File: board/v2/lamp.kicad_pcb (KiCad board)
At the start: 4 copper layers, 28 x 28 mm, 42 parts, among them J1 Conn_01x01_Female, J2 Conn_01x01_Female, J3 Conn_01x01_Female, J4 Conn_01x01_Female, J5 Conn_01x01_Female, J6 Conn_01x01_Female, J7 Conn_01x01_Female, J8 Conn_ARM_JTAG_SWD_10, Q1 SIA483DJ-T1-GE3‎, U1 STM32G071GxU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

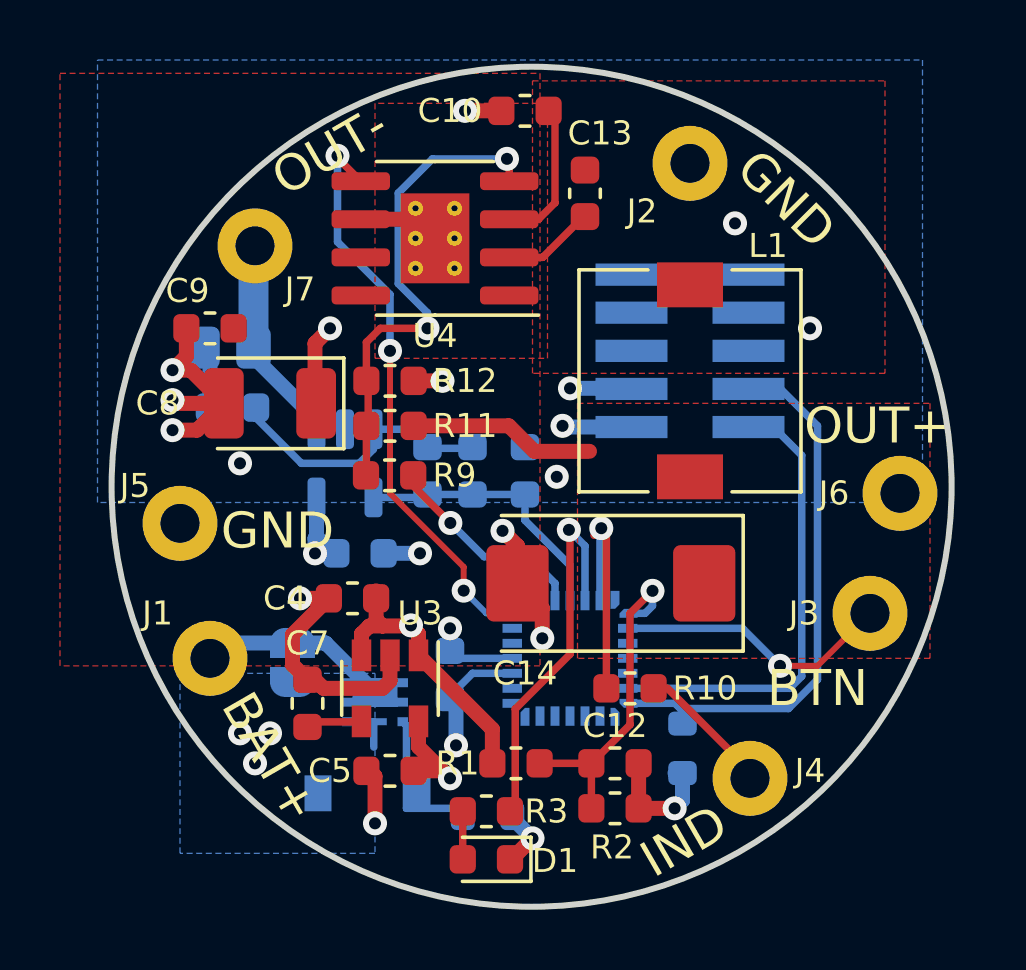
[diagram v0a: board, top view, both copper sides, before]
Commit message: hw: Fix RESET line on JTAG connector
Previously this was disconnected due to a net name mismatch.
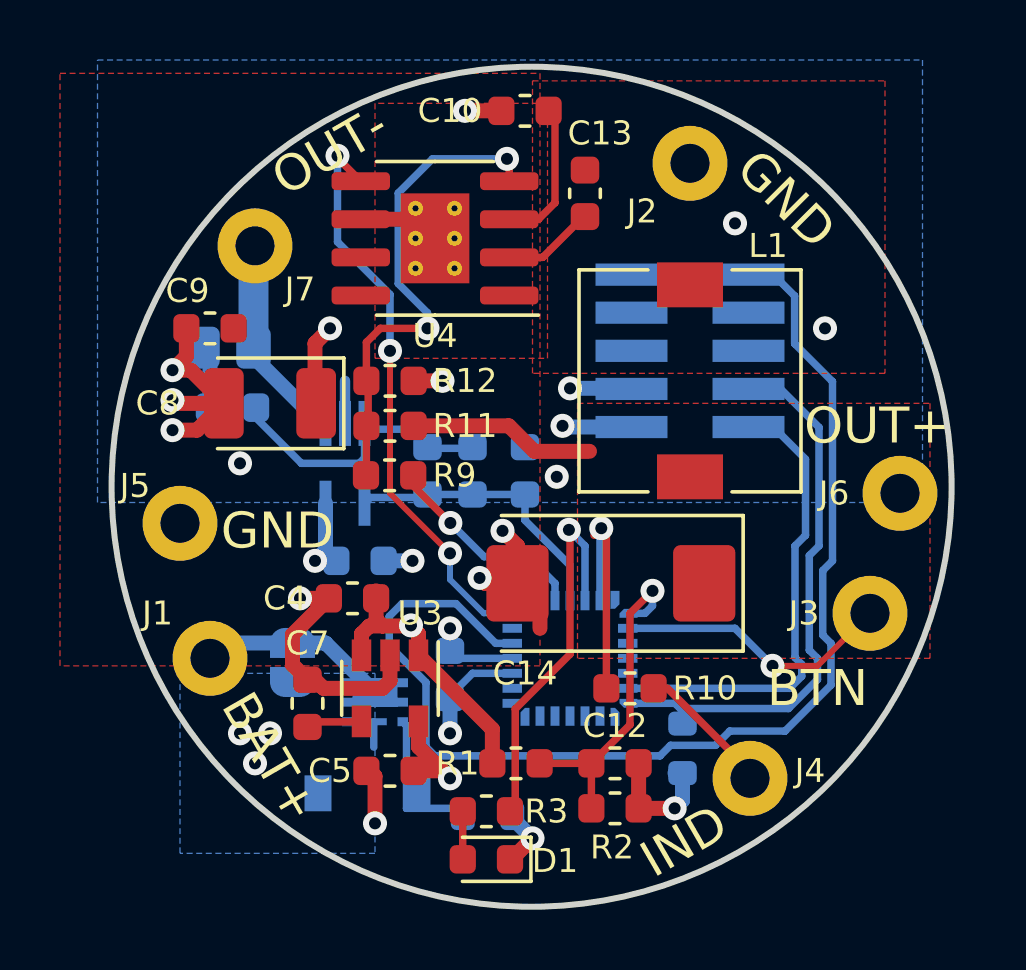
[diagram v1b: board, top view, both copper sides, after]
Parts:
- U2: footprint Package_TO_SOT_SMD:SOT-23-5 -> Package_TO_SOT_SMD:SOT-353_SC-70-5_Handsoldering
- moved C11 0.25 mm to (130.0, 86.2)
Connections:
- U1 pad 5: /RESET -> /~{RESET}
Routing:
- net /~{RESET}: track 0.00 -> 39.9 mm
- net GND: track 40.0 -> 42.2 mm
- net +3V3: track 13.9 -> 13.2 mm

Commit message: hw: Larger package for LDO input cap
0603 was too small for a realistic capacitance.
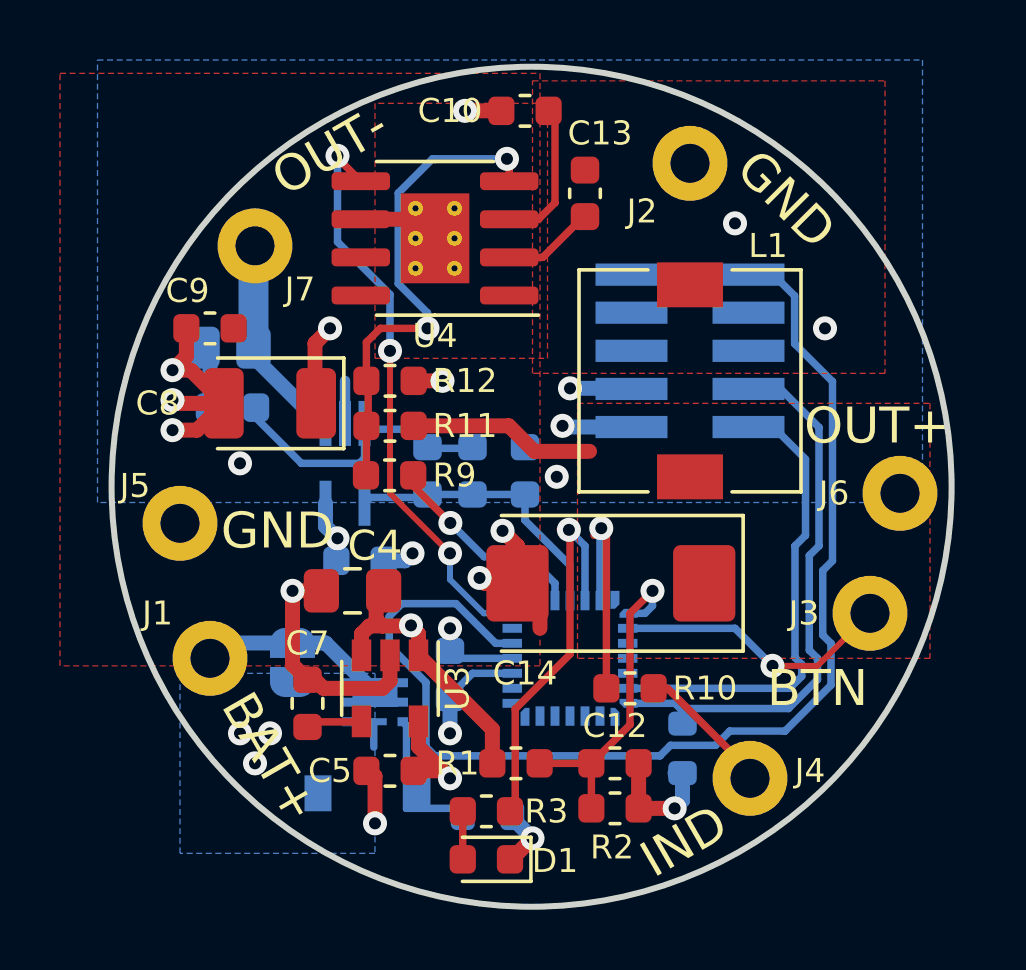
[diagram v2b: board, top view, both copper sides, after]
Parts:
- C4: footprint Capacitor_SMD:C_0603_1608Metric -> Capacitor_SMD:C_0805_2012Metric_Pad1.18x1.45mm_HandSolder
- moved C4 0.25 mm to (129.8, 87.2)
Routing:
- net +3V3: track 13.2 -> 12.5 mm
